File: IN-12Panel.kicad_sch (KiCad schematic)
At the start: 8 parts, among them J1 Conn_01x04_Pin, J2 Conn_01x04_Pin, J3 Conn_01x11_Pin, J4 Conn_01x11_Pin, U1 IN-12, U2 IN-12, U3 IN-12, U4 IN-12

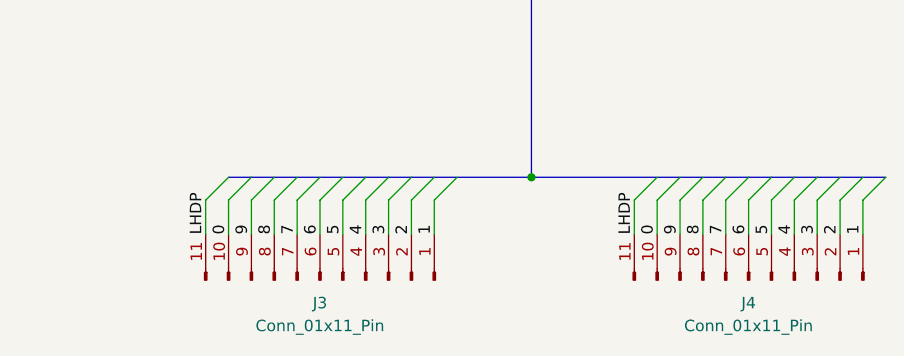
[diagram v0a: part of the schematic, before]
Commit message: 基板結合にあたり，コネクタの位置・向きを変更
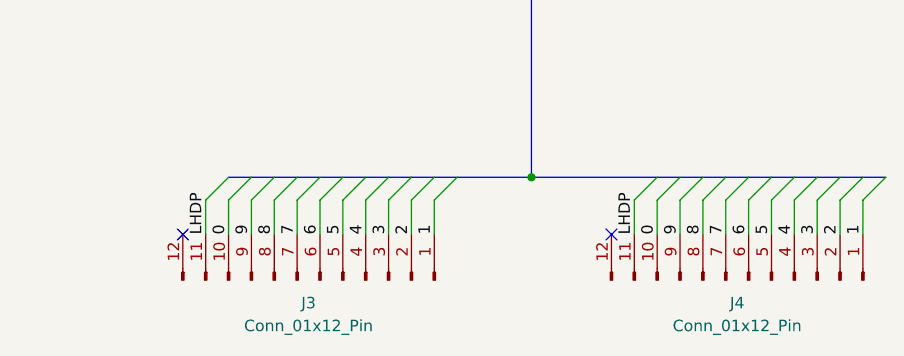
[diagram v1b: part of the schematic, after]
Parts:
- removed J3, J4: Conn_01x11_Pin, Connector_JST:JST_XH_S11B-XH-A_1x11_P2.50mm_Horizontal, symbol Connector:Conn_01x11_Pin
- added J3, J4: Conn_01x12_Pin, Connector_JST:JST_XH_S12B-XH-A_1x12_P2.50mm_Horizontal, symbol Connector:Conn_01x12_Pin
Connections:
- net 0: now also J3.10 (Pin_10), J4.10 (Pin_10)
- net 1: now also J3.1 (Pin_1), J4.1 (Pin_1)
- net 2: now also J3.2 (Pin_2), J4.2 (Pin_2)
- net 3: now also J3.3 (Pin_3), J4.3 (Pin_3)
- net 4: now also J3.4 (Pin_4), J4.4 (Pin_4)
- net 5: now also J3.5 (Pin_5), J4.5 (Pin_5)
- net 6: now also J3.6 (Pin_6), J4.6 (Pin_6)
- net 7: now also J3.7 (Pin_7), J4.7 (Pin_7)
- net 8: now also J3.8 (Pin_8), J4.8 (Pin_8)
- net 9: now also J3.9 (Pin_9), J4.9 (Pin_9)
- net LHDP: now also J3.11 (Pin_11), J4.11 (Pin_11)
- no-connect marks 0 -> 2
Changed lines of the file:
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@@
   (junction (at 62.23 57.785) (diameter 0) (color 0 0 0 0)
   )
+  (no_connect (at 244.475 126.365))
+  (no_connect (at 196.85 126.365))
   (bus_entry (at 50.8 81.28) (size 2.54 2.54)
     (stroke (width 0) (type default))
@@
     (effects (font (size 1.27 1.27)) (justify left bottom))
   )
-  (symbol (lib_id "Connector:Conn_01x11_Pin") (at 259.715 131.445 270) (mirror x) (unit 1)
-    (in_bom yes) (on_board yes) (dnp no)
-    (property "Reference" "J4" (at 259.715 133.985 90)
+  (symbol (lib_id "Connector:Conn_01x12_Pin") (at 259.715 131.445 270) (mirror x) (unit 1)
+    (in_bom yes) (on_board yes) (dnp no) (fields_autoplaced)
+    (property "Reference" "J4" (at 258.445 133.985 90)
       (effects (font (size 1.27 1.27)))
     )
-    (property "Value" "Conn_01x11_Pin" (at 259.715 136.525 90)
+    (property "Value" "Conn_01x12_Pin" (at 258.445 136.525 90)
       (effects (font (size 1.27 1.27)))
     )
-    (property "Footprint" "Connector_JST:JST_XH_S11B-XH-A_1x11_P2.50mm_Horizontal" (at 259.715 131.445 0)
+    (property "Footprint" "Connector_JST:JST_XH_S12B-XH-A_1x12_P2.50mm_Horizontal" (at 259.715 131.445 0)
       (effects (font (size 1.27 1.27)) hide)
     )
@@
     (pin "10")
     (pin "11")
+    (pin "12")
     (pin "2")
     (pin "3")
@@
         (path "/77b60d2b-416f-4a90-bee0-0c4aafa60082"
           (reference "J2") (unit 1)
+        )
+      )
+    )
+  )
+  (symbol (lib_id "Connector:Conn_01x12_Pin") (at 212.09 131.445 270) (mirror x) (unit 1)
+    (in_bom yes) (on_board yes) (dnp no) (fields_autoplaced)
+    (property "Reference" "J3" (at 210.82 133.985 90)
+      (effects (font (size 1.27 1.27)))
+    )
+    (property "Value" "Conn_01x12_Pin" (at 210.82 136.525 90)
+      (effects (font (size 1.27 1.27)))
+    )
+    (property "Footprint" "Connector_JST:JST_XH_S12B-XH-A_1x12_P2.50mm_Horizontal" (at 212.09 131.445 0)
+      (effects (font (size 1.27 1.27)) hide)
+    )
+    (property "Datasheet" "~" (at 212.09 131.445 0)
+      (effects (font (size 1.27 1.27)) hide)
+    )
+    (pin "1")
+    (pin "10")
+    (pin "11")
+    (pin "12")
+    (pin "2")
+    (pin "3")
+    (pin "4")
+    (pin "5")
+    (pin "6")
+    (pin "7")
+    (pin "8")
+    (pin "9")
+    (instances
+      (project "IN-12Panel"
+        (path "/77b60d2b-416f-4a90-bee0-0c4aafa60082"
+          (reference "J3") (unit 1)
         )
       )
@@
         )
       )
-    )
-  )
-  (symbol (lib_id "Connector:Conn_01x11_Pin") (at 212.09 131.445 270) (mirror x) (unit 1)
-    (in_bom yes) (on_board yes) (dnp no)
-    (property "Reference" "J3" (at 212.09 133.985 90)
-      (effects (font (size 1.27 1.27)))
-    )
-    (property "Value" "Conn_01x11_Pin" (at 212.09 136.525 90)
-      (effects (font (size 1.27 1.27)))
-    )
-    (property "Footprint" "Connector_JST:JST_XH_S11B-XH-A_1x11_P2.50mm_Horizontal" (at 212.09 131.445 0)
-      (effects (font (size 1.27 1.27)) hide)
-    )
-    (property "Datasheet" "~" (at 212.09 131.445 0)
-      (effects (font (size 1.27 1.27)) hide)
-    )
-    (pin "1")
-    (pin "10")
-    (pin "11")
-    (pin "2")
-    (pin "3")
-    (pin "4")
-    (pin "5")
-    (pin "6")
-    (pin "7")
-    (pin "8")
-    (pin "9")
-    (instances
-      (project "IN-12Panel"
-        (path "/77b60d2b-416f-4a90-bee0-0c4aafa60082"
-          (reference "J3") (unit 1)
-        )
-      )
